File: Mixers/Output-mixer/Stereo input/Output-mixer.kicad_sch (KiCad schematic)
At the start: 132 parts, among them J1 In, J10 In, J11 In, J12 In, J13 Power Input, J14 Conn_01x04_Female, J15 Conn_01x02_Male, J16 Conn_01x04_Male, J17 Conn_01x02_Female, J18 OutR, J19 OutL, J2 In, J20 Jack 3.5 Out, J21 Jack 3.5 Out, J22 OutL, J23 OutR, J3 In, J4 In, J5 In, J6 In, J7 In, J8 In, J9 In, SW1 Mute, SW2 Mute, SW3 Mute, SW4 Mute, SW5 Mute, SW6 Mute, U1 TL072, U2 TL072, U3 TL072, U4 TL072

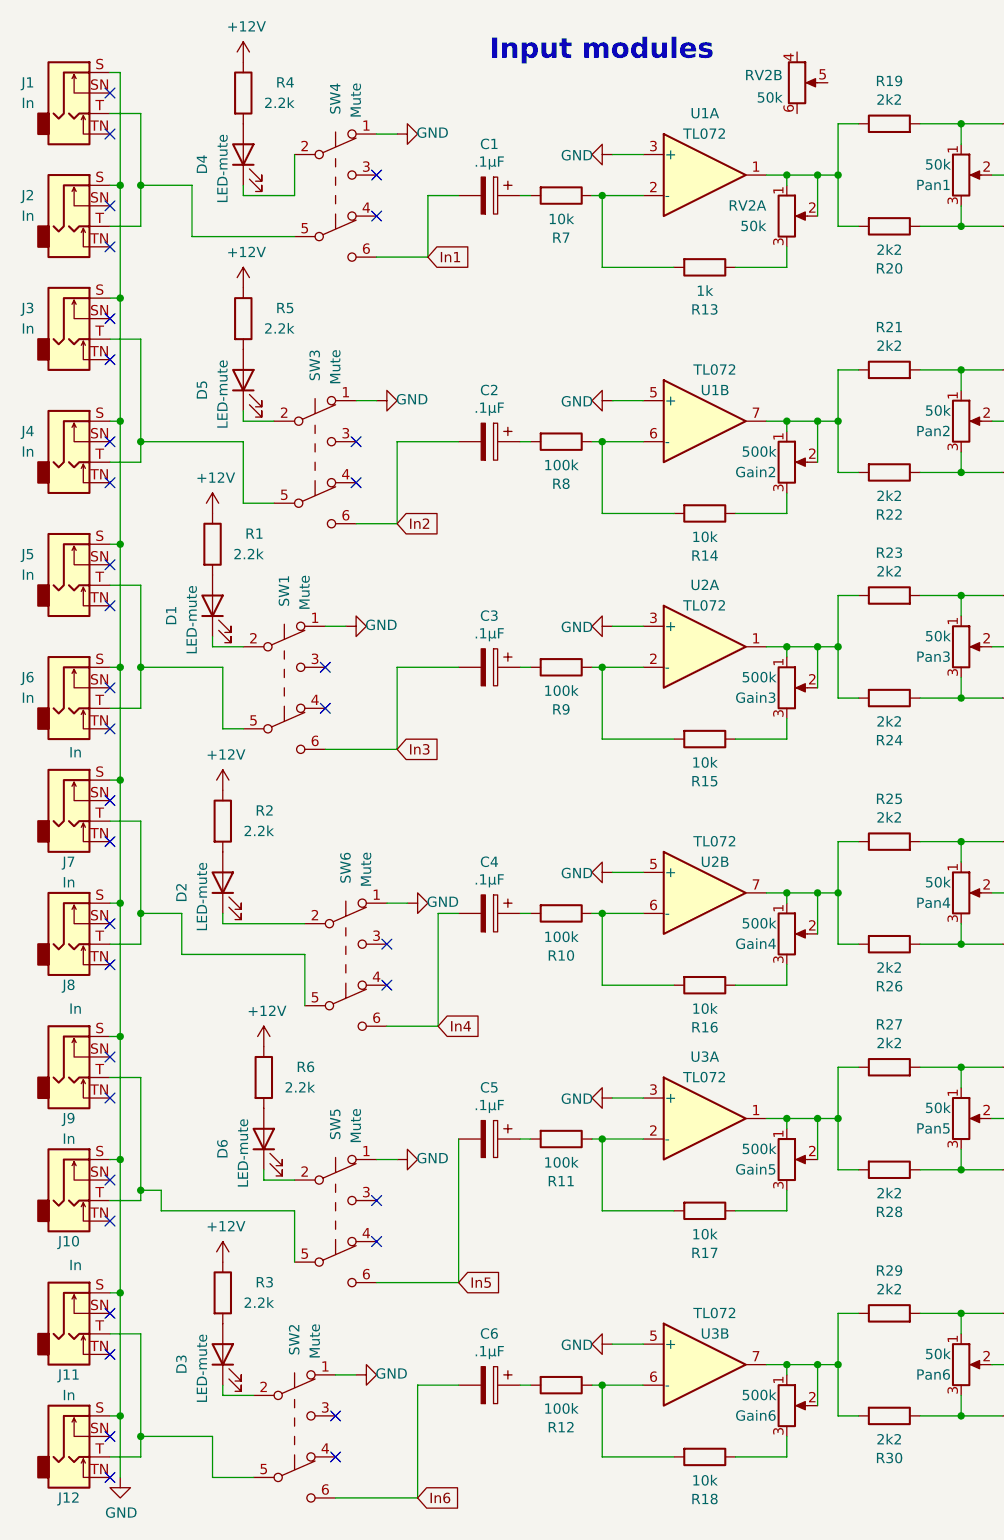
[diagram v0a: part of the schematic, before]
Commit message: update stereo output mixer
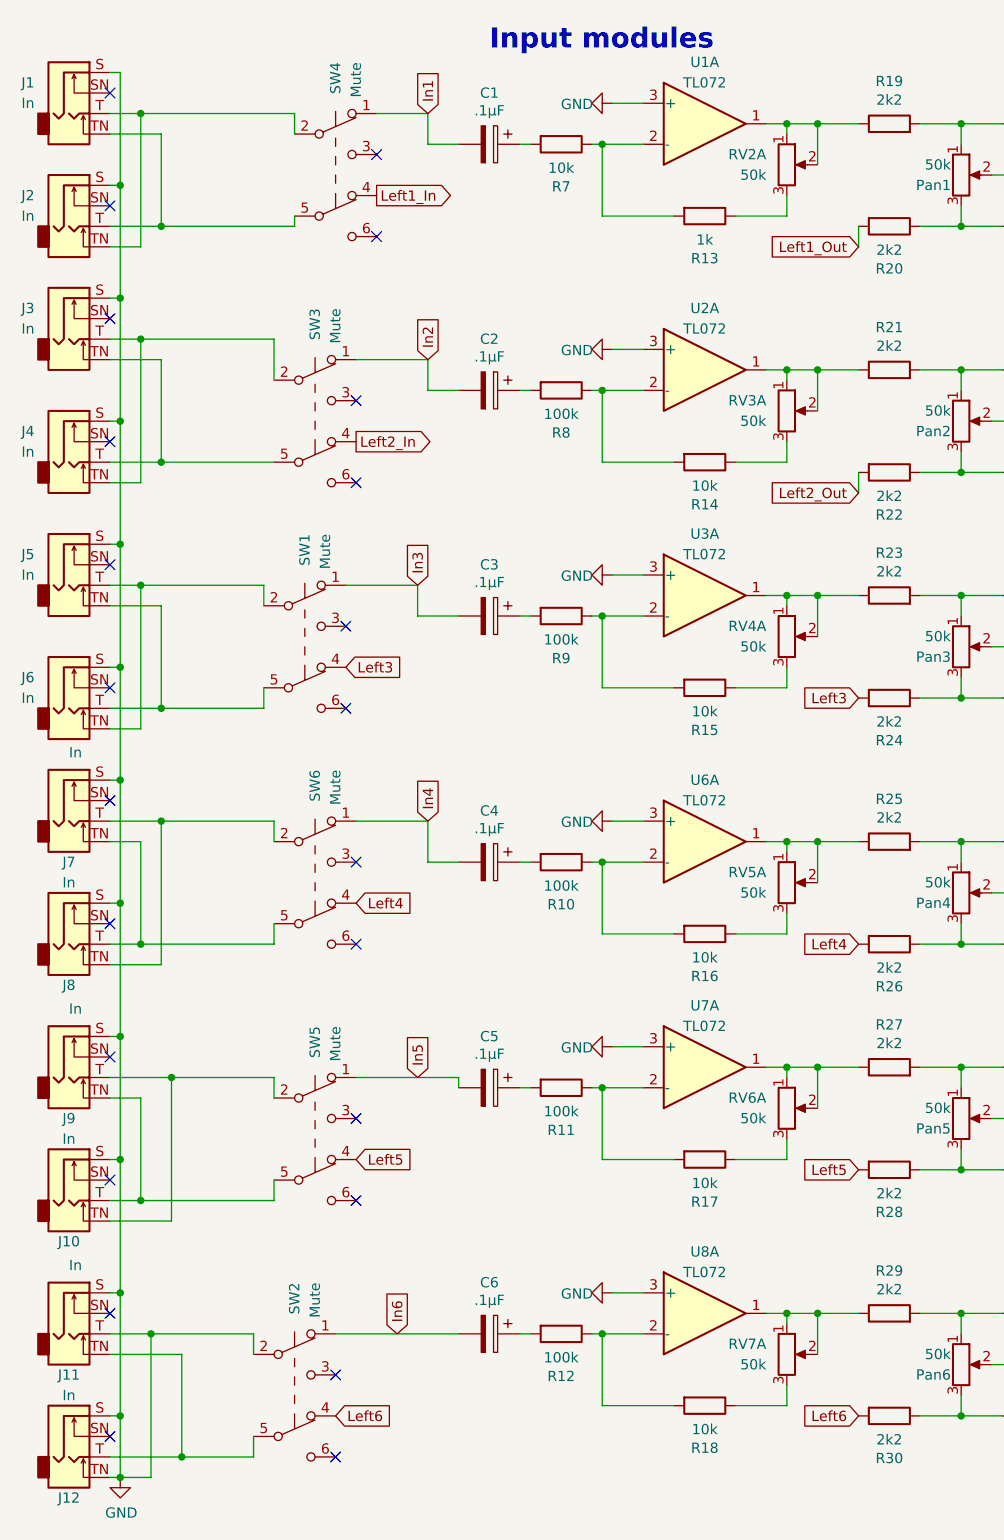
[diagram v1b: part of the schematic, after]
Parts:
- removed D1, D2, D3, D4, D5, D6: LED-mute, LED_THT:LED_D4.0mm, symbol Device:LED
- removed Gain2, Gain3, Gain4, Gain5, Gain6: 500k, Synth:Pot-bourns-alpha, symbol Device:R_POT
- removed R1, R2, R3, R4, R5, R6: 2.2k, Resistor_THT:R_Axial_DIN0207_L6.3mm_D2.5mm_P10.16mm_Horizontal, symbol Device:R
- removed unit 2 of RV2
- removed unit 2 of U1
- removed unit 2 of U2
- removed unit 1 of U3
- removed unit 2 of U3
- added RV3, RV4, RV5, RV6, RV7: 50k, Synth:PTV1124420AA503, symbol Device:R_Potentiometer_Dual_Separate
- added unit 1 of U2
- added U6, U7, U8: TL072, Package_DIP:DIP-8_W7.62mm_Socket, symbol Amplifier_Operational:TL072
- renumbered U2 to U3
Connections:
- net GND: now also J11.T, J12.TN, SW2.2 (B), U2.3 (+), U6.3 (+), U7.3 (+), U8.3 (+); no longer SW1.1 (A), SW2.1 (A), SW3.1 (A), SW4.1 (A), SW5.1 (A), SW6.1 (A)
- net In1: now also SW4.1 (A); no longer SW4.6 (C)
- net In2: now also SW3.1 (A); no longer SW3.6 (C)
- net In3: now also SW1.1 (A); no longer SW1.6 (C)
- net In4: now also SW6.1 (A); no longer SW6.6 (C)
- net In5: now also SW5.1 (A); no longer SW5.6 (C)
- net In6: now also SW2.1 (A); no longer SW2.6 (C)
- net at R27.1: now also RV6.1, RV6.2, U7.1; no longer R28.2
- net at R11.1, R17.2: now also U7.2 (-)
- net at R14.2, R8.1: now also U2.2 (-)
- net at R21.1: now also RV3.1, RV3.2, U2.1; no longer R22.2
- net at R19.1, RV2.1, RV2.2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: no longer R20.2
- net at SW4.2 (B): now also J1.T, J2.TN
- net Left1_In: now reaches SW4.4 (A)
- net at J2.T, SW4.5 (B): now also J1.TN; no longer J1.T
- net at SW1.2 (B): now also J5.T, J6.TN
- net Left3: now reaches SW1.4 (A)
- net Left3: now also R24.2
- net at J6.T, SW1.5 (B): now also J5.TN; no longer J5.T
- net at J8.T, SW6.5 (B): now also J7.TN; no longer J7.T
- net at J8.TN: now also J7.T, SW6.2 (B)
- net at J10.T, SW5.5 (B): now also J9.TN; no longer J9.T
- net at J10.TN: now also J9.T, SW5.2 (B)
- net at R12.1, R18.2: now also U8.2 (-)
- net at R17.1: now also RV6.3
- net at R29.1: now also RV7.1, RV7.2, U8.1; no longer R30.2
- net at R23.1, U3.1: now also RV4.1, RV4.2; no longer R24.2
- net at R25.1: now also RV5.1, RV5.2, U6.1; no longer R26.2
- net at J12.T, SW2.5 (B): now also J11.TN; no longer J11.T
- net Left6: now reaches SW2.4 (A)
- net Left6: now also R30.2
- net Left5: now reaches SW5.4 (A)
- net Left5: now also R28.2
- net at J4.T, SW3.5 (B): now also J3.TN; no longer J3.T
- net at J4.TN: now also J3.T, SW3.2 (B)
- net at R14.1: now also RV3.3
- net Left2_In: now reaches SW3.4 (A)
- net at R15.1: now also RV4.3
- net at R10.1, R16.2: now also U6.2 (-)
- net at R16.1: now also RV5.3
- net at R18.1: now also RV7.3
- net Left4: now reaches SW6.4 (A)
- net Left4: now also R26.2
- new net Left1_Out: R20.2
- new net Left2_Out: R22.2
- no-connect marks 46 -> 34
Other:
- moved on the sheet: C1, C2, C3, C4, C5, C6, R10, R11, R12, R13, R14, R15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

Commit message: finish schem update
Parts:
- renumbered RV2 to RV8
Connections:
- net Left3 renamed Left3_In
- net Left3_In: no longer R24.2
- net Left4 renamed Left4_In
- net Left4_In: no longer R26.2
- net Left5 renamed Left5_In
- net Left5_In: no longer R28.2
- net Left6 renamed Left6_In
- net Left6_In: no longer R30.2
- new net Left3_Out: R24.2
- new net Left4_Out: R26.2
- new net Left5_Out: R28.2
- new net Left6_Out: R30.2

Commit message: update schem (not finished)
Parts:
- added unit 2 of RV8
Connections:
- net Left1_Out: now also RV8.4, RV8.5
- net at RV8.3: no longer R13.1
- net Right1_Out: now reaches R19.1, RV8.1, RV8.2, U1.1
- net In1 renamed Right1_In
- net In2 renamed Right2_In
- net In3 renamed Right3_In
- net In4 renamed Right4_In
- net In5 renamed Right5_In
- net In6 renamed Right6_In
- new net Right1_GOut: R13.1
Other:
- moved on the sheet: Pan1, R13, R19, R20, RV8A, SW4

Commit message: finish update schem
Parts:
- removed unit 2 of RV8
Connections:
- net Right1_GOut: now also RV8.3
- net Right6_Out: now reaches R29.1, RV7.1, RV7.2, U8.1
- net Right4_Out: now reaches R25.1, RV5.1, RV5.2, U6.1
- net Right4_GOut: now reaches R16.1, RV5.3
- net Right5_Out: now reaches R27.1, RV6.1, RV6.2, U7.1
- net Right5_GOut: now reaches R17.1, RV6.3
- net Right3_Out: now reaches R23.1, RV4.1, RV4.2, U3.1
- net Right2_GOut: now reaches R14.1, RV3.3
- net Right3_GOut: now reaches R15.1, RV4.3
- net Right2_Out: now reaches R21.1, RV3.1, RV3.2, U2.1
- net Right6_GOut: now reaches R18.1, RV7.3
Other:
- moved on the sheet: R14, R16, R18, RV8A

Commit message: early board update
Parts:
- renumbered Pan2 to Pan1, Pan3 to Pan2, Pan4 to Pan3, Pan5 to Pan4, Pan6 to Pan5, Pan1 to Pan6, R7 to R1, R13 to R10, R15 to R11, R17 to R12, R21 to R13, R22 to R14, R23 to R15, R24 to R16, R25 to R17, R26 to R18, R27 to R19, R8 to R2, R28 to R20, R29 to R21, R30 to R22, R19 to R23, R20 to R24, R31 to R25, R32 to R26, R33 to R27, R34 to R28, R35 to R29, R9 to R3, R36 to R30, R37 to R31, R38 to R32, R39 to R33, R40 to R34, R41 to R35, R42 to R36, R43 to R37, R44 to R38, R45 to R39, R10 to R4, R46 to R40, R47 to R41, R48 to R42, R49 to R43, R50 to R44, R11 to R5, R12 to R6, R16 to R7, R14 to R8, R18 to R9, RV8 to RV1, RV3 to RV2, RV4 to RV3, RV5 to RV4, RV6 to RV5, RV7 to RV6, RV1 to RV7, SW2 to SW1, SW4 to SW2, SW1 to SW3, SW3 to SW4, SW6 to SW5, SW5 to SW6, U6 to U4, U7 to U5, U8 to U6, U4 to U7

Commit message: finish updating PCB
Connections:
- net GND: no longer J11.T, J12.TN, SW1.2 (B)
- new net: J11.T, J12.TN, SW1.2 (B)
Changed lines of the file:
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@@
   (junction (at 82.55 86.36) (diameter 0) (color 0 0 0 0)
   )
-  (junction (at 22.86 193.04) (diameter 0) (color 0 0 0 0)
-  )
   (junction (at 260.35 93.98) (diameter 0) (color 0 0 0 0)
   )
@@
     (stroke (width 0) (type default) (color 0 0 0 0))
   )
-  (wire (pts (xy 21.59 193.04) (xy 22.86 193.04))
-    (stroke (width 0) (type default) (color 0 0 0 0))
-  )
   (wire (pts (xy 165.1 45.72) (xy 165.1 43.18))
     (stroke (width 0) (type default) (color 0 0 0 0))
@@
     (stroke (width 0) (type default) (color 0 0 0 0))
   )
-  (wire (pts (xy 22.86 185.42) (xy 22.86 193.04))
+  (wire (pts (xy 22.86 185.42) (xy 22.86 195.58))
     (stroke (width 0) (type default) (color 0 0 0 0))
   )
@@
     (stroke (width 0) (type default) (color 0 0 0 0))
   )
-  (wire (pts (xy 22.86 193.04) (xy 26.67 193.04))
+  (wire (pts (xy 21.59 193.04) (xy 26.67 193.04))
     (stroke (width 0) (type default) (color 0 0 0 0))
   )
@@
       (effects (font (size 1.27 1.27)) hide)
     )
-    (pin "1")
-    (pin "2")
-    (pin "3")
-    (pin "5")
-    (pin "6")
-    (pin "7")
     (pin "4")
     (pin "8")
@@
     (pin "2")
     (pin "3")
-    (pin "4")
-    (pin "5")
-    (pin "6")
   )
   (symbol (lib_id "Connector:AudioJack2_Switch") (at 16.51 158.75 0) (unit 1)
@@
     (pin "2")
     (pin "3")
-    (pin "4")
-    (pin "5")
-    (pin "6")
   )
   (symbol (lib_id "power:+12V") (at 247.65 25.4 0) (unit 1)
@@
     (pin "2")
     (pin "3")
-    (pin "4")
-    (pin "5")
-    (pin "6")
   )
   (symbol (lib_id "Device:R") (at 93.98 35.56 270) (unit 1)
@@
       (effects (font (size 1.27 1.27)) hide)
     )
-    (pin "1")
-    (pin "2")
-    (pin "3")
-    (pin "5")
-    (pin "6")
-    (pin "7")
     (pin "4")
     (pin "8")
@@
     (pin "2")
     (pin "3")
-    (pin "5")
-    (pin "6")
-    (pin "7")
-    (pin "4")
-    (pin "8")
   )
   (symbol (lib_id "Device:C_Small") (at 212.09 45.72 0) (unit 1)
@@
     (pin "2")
     (pin "3")
-    (pin "5")
-    (pin "6")
-    (pin "7")
-    (pin "4")
-    (pin "8")
   )
   (symbol (lib_id "Device:C_Small") (at 181.61 33.02 0) (unit 1)
@@
     (pin "2")
     (pin "3")
-    (pin "4")
-    (pin "5")
-    (pin "6")
   )
   (symbol (lib_id "Device:R") (at 135.89 185.42 270) (unit 1)
@@
     (pin "2")
     (pin "3")
-    (pin "5")
-    (pin "6")
-    (pin "7")
-    (pin "4")
-    (pin "8")
   )
   (symbol (lib_id "Device:CP") (at 214.63 72.39 90) (unit 1)
@@
       (effects (font (size 1.27 1.27)) hide)
     )
-    (pin "1")
-    (pin "2")
-    (pin "3")
     (pin "4")
     (pin "5")
@@
     (pin "2")
     (pin "3")
-    (pin "4")
-    (pin "5")
-    (pin "6")
   )
   (symbol (lib_id "Switch:SW_Push_DPDT") (at 46.99 62.23 0) (unit 1)
@@
     (pin "2")
     (pin "3")
-    (pin "4")
-    (pin "5")
-    (pin "6")
   )
   (symbol (lib_id "Amplifier_Operational:TL072") (at 95.25 25.4 0) (unit 1)
@@
     (pin "2")
     (pin "3")
-    (pin "5")
-    (pin "6")
-    (pin "7")
-    (pin "4")
-    (pin "8")
   )
   (symbol (lib_id "Device:R") (at 194.31 115.57 270) (unit 1)
@@
     (pin "2")
     (pin "3")
-    (pin "5")
-    (pin "6")
-    (pin "7")
-    (pin "4")
-    (pin "8")
   )
   (symbol (lib_id "Device:R") (at 135.89 83.82 90) (unit 1)
@@
     (pin "2")
   )
-  (symbol (lib_id "power:GND") (at 22.86 193.04 0) (unit 1)
+  (symbol (lib_id "power:GND") (at 22.86 195.58 90) (unit 1)
     (in_bom yes) (on_board yes)
-    (property "Reference" "#PWR01" (id 0) (at 22.86 199.39 0)
+    (property "Reference" "#PWR01" (id 0) (at 29.21 195.58 0)
       (effects (font (size 1.27 1.27)) hide)
     )
-    (property "Value" "GND" (id 1) (at 22.987 197.4342 0))
-    (property "Footprint" "" (id 2) (at 22.86 193.04 0)
+    (property "Value" "GND" (id 1) (at 27.2542 195.453 0))
+    (property "Footprint" "" (id 2) (at 22.86 195.58 0)
       (effects (font (size 1.27 1.27)) hide)
     )
-    (property "Datasheet" "" (id 3) (at 22.86 193.04 0)
+    (property "Datasheet" "" (id 3) (at 22.86 195.58 0)
       (effects (font (size 1.27 1.27)) hide)
     )
@@
       (effects (font (size 1.27 1.27)) hide)
     )
-    (pin "1")
-    (pin "2")
-    (pin "3")
-    (pin "5")
-    (pin "6")
-    (pin "7")
     (pin "4")
     (pin "8")
@@
     (pin "2")
     (pin "3")
-    (pin "5")
-    (pin "6")
-    (pin "7")
-    (pin "4")
-    (pin "8")
   )
   (symbol (lib_id "Device:R") (at 118.11 55.88 90) (unit 1)
@@
       (effects (font (size 1.27 1.27)) hide)
     )
-    (pin "1")
-    (pin "2")
-    (pin "3")
     (pin "5")
     (pin "6")
     (pin "7")
-    (pin "4")
-    (pin "8")
   )
   (symbol (lib_id "Device:R") (at 77.47 116.84 270) (unit 1)
@@
       (effects (font (size 1.27 1.27)) hide)
     )
-    (pin "1")
-    (pin "2")
-    (pin "3")
-    (pin "5")
-    (pin "6")
-    (pin "7")
     (pin "4")
     (pin "8")
@@
     (pin "2")
     (pin "3")
-    (pin "4")
-    (pin "5")
-    (pin "6")
   )
   (symbol (lib_id "Device:C_Small") (at 191.77 45.72 0) (unit 1)
@@
     (pin "2")
     (pin "3")
-    (pin "5")
-    (pin "6")
-    (pin "7")
-    (pin "4")
-    (pin "8")
   )
   (symbol (lib_id "Device:C_Small") (at 181.61 45.72 0) (unit 1)
